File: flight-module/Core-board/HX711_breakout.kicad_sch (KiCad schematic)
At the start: 10 parts

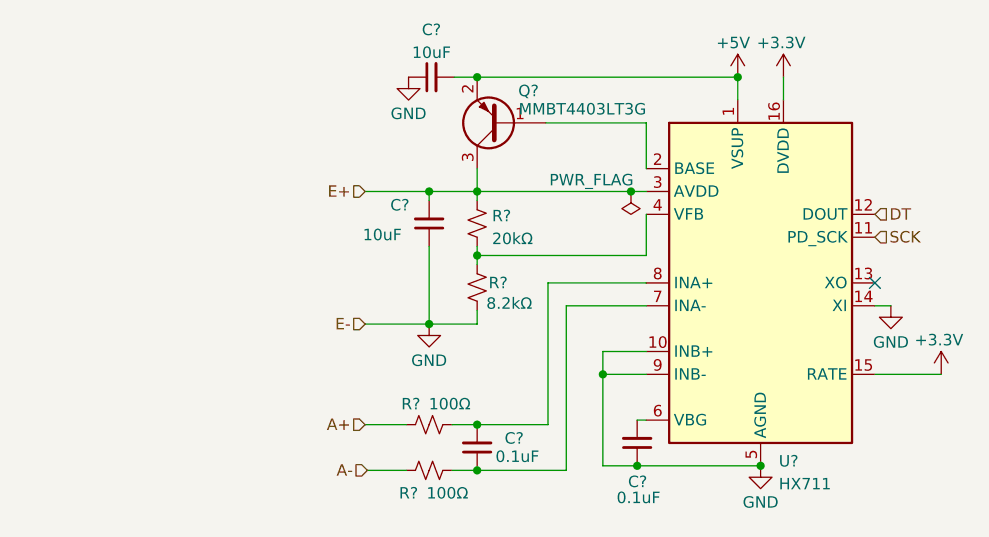
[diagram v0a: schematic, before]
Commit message: worked on core-board schematic. Not done.
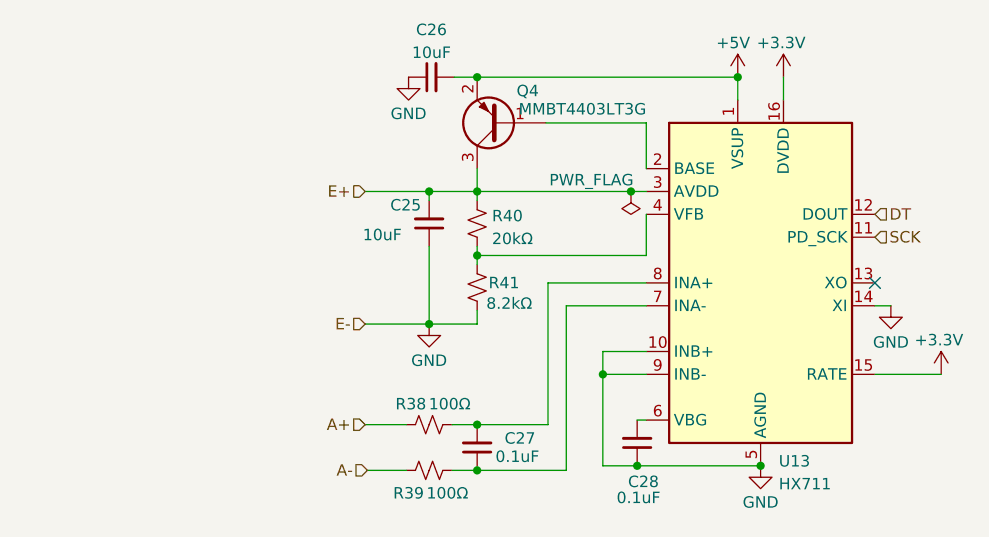
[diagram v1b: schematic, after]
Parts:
- gave numbers to parts that had none: 10

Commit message: Progress on core board.
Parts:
- added J5: Conn_01x03_Pin, Connector_PinHeader_2.54mm:PinHeader_1x03_P2.54mm_Vertical, symbol Connector:Conn_01x03_Pin
- renumbered C25 to C17, C26 to C18, C27 to C19, C28 to C20, R38 to R27, R39 to R28, R40 to R29, R41 to R30, U13 to U5
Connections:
- net A+: now also J5.3 (Pin_3)
- net E+: now also J5.1 (Pin_1)
- net GND: now also J5.2 (Pin_2)
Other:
- moved on the sheet: C17, C18, C20, Q4, R29, U5

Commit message: Finished flight-core.
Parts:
- added R1: 100kΩ, Resistor_SMD:R_0603_1608Metric, symbol Device:R_Small_US
- added R4: 2kΩ, Resistor_SMD:R_0603_1608Metric, symbol Device:R_Small_US
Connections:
- net A+: now also R1.1; no longer R27.2
- net GND: now also R4.1
- new net: R1.2, R27.2, R4.2
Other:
- moved on the sheet: J5
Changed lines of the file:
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@@
   (junction (at 116.84 40.64) (diameter 0) (color 0 0 0 0)
   )
+  (junction (at 76.2 68.58) (diameter 0) (color 0 0 0 0)
+  )
   (junction (at 86.36 60.96) (diameter 0) (color 0 0 0 0)
   )
@@
   )
   (junction (at 86.36 40.64) (diameter 0) (color 0 0 0 0)
+  )
+  (junction (at 76.2 78.74) (diameter 0) (color 0 0 0 0)
   )
   (junction (at 119.38 83.82) (diameter 0) (color 0 0 0 0)
@@
     (stroke (width 0) (type default))
   )
-  (wire (pts (xy 73.66 78.74) (xy 78.74 78.74))
-    (stroke (width 0) (type default))
-  )
   (wire (pts (xy 86.36 68.58) (xy 81.28 68.58))
     (stroke (width 0) (type default))
@@
     (stroke (width 0) (type default))
   )
-  (wire (pts (xy 73.66 68.58) (xy 81.28 68.58))
-    (stroke (width 0) (type default))
-  )
   (wire (pts (xy 86.36 60.96) (xy 106.68 60.96))
     (stroke (width 0) (type default))
@@
     (stroke (width 0) (type default))
   )
+  (wire (pts (xy 76.2 78.74) (xy 78.74 78.74))
+    (stroke (width 0) (type default))
+  )
   (wire (pts (xy 106.68 55.88) (xy 106.68 60.96))
     (stroke (width 0) (type default))
   )
+  (wire (pts (xy 76.2 68.58) (xy 76.2 71.12))
+    (stroke (width 0) (type default))
+  )
   (wire (pts (xy 86.36 40.64) (xy 116.84 40.64))
     (stroke (width 0) (type default))
@@
     (stroke (width 0) (type default))
   )
+  (wire (pts (xy 68.58 78.74) (xy 71.12 78.74))
+    (stroke (width 0) (type default))
+  )
   (wire (pts (xy 86.36 78.74) (xy 93.98 78.74))
     (stroke (width 0) (type default))
@@
     (stroke (width 0) (type default))
   )
+  (wire (pts (xy 76.2 76.2) (xy 76.2 78.74))
+    (stroke (width 0) (type default))
+  )
   (wire (pts (xy 86.36 53.34) (xy 104.14 53.34))
     (stroke (width 0) (type default))
@@
     (stroke (width 0) (type default))
   )
+  (wire (pts (xy 73.66 68.58) (xy 76.2 68.58))
+    (stroke (width 0) (type default))
+  )
   (wire (pts (xy 96.52 66.04) (xy 106.68 66.04))
     (stroke (width 0) (type default))
   )
+  (wire (pts (xy 76.2 68.58) (xy 81.28 68.58))
+    (stroke (width 0) (type default))
+  )
   (wire (pts (xy 104.14 83.82) (xy 119.38 83.82))
     (stroke (width 0) (type default))
@@
     (stroke (width 0) (type default))
   )
-  (hierarchical_label "E+" (shape input) (at 40.64 39.37 180) (fields_autoplaced)
+  (hierarchical_label "E+" (shape input) (at 40.64 40.64 180) (fields_autoplaced)
     (effects (font (size 1.27 1.27)) (justify right))
   )
-  (hierarchical_label "E-" (shape input) (at 40.64 41.91 180) (fields_autoplaced)
+  (hierarchical_label "E-" (shape input) (at 40.64 43.18 180) (fields_autoplaced)
     (effects (font (size 1.27 1.27)) (justify right))
   )
-  (hierarchical_label "A+" (shape input) (at 40.64 44.45 180) (fields_autoplaced)
-    (effects (font (size 1.27 1.27)) (justify right))
-  )
-  (hierarchical_label "A+" (shape input) (at 73.66 78.74 180) (fields_autoplaced)
+  (hierarchical_label "A+" (shape input) (at 40.64 45.72 180) (fields_autoplaced)
     (effects (font (size 1.27 1.27)) (justify right))
   )
@@
     (effects (font (size 1.27 1.27)) (justify right))
   )
+  (hierarchical_label "E+" (shape input) (at 73.66 53.34 180) (fields_autoplaced)
+    (effects (font (size 1.27 1.27)) (justify right))
+  )
+  (hierarchical_label "A+" (shape input) (at 68.58 78.74 180) (fields_autoplaced)
+    (effects (font (size 1.27 1.27)) (justify right))
+  )
+  (hierarchical_label "DT" (shape input) (at 132.08 55.88 0) (fields_autoplaced)
+    (effects (font (size 1.27 1.27)) (justify left))
+  )
   (hierarchical_label "E-" (shape input) (at 73.66 68.58 180) (fields_autoplaced)
     (effects (font (size 1.27 1.27)) (justify right))
   )
-  (hierarchical_label "E+" (shape input) (at 73.66 53.34 180) (fields_autoplaced)
-    (effects (font (size 1.27 1.27)) (justify right))
-  )
-  (hierarchical_label "DT" (shape input) (at 132.08 55.88 0) (fields_autoplaced)
-    (effects (font (size 1.27 1.27)) (justify left))
+  (symbol (lib_id "Device:R_Small_US") (at 73.66 78.74 90) (unit 1)
+    (in_bom yes) (on_board yes) (dnp no)
+    (property "Reference" "R1" (at 69.85 74.422 90)
+      (effects (font (size 1.27 1.27)))
+    )
+    (property "Value" "100kΩ" (at 70.358 76.454 90)
+      (effects (font (size 1.27 1.27)))
+    )
+    (property "Footprint" "Resistor_SMD:R_0603_1608Metric" (at 73.66 78.74 0)
+      (effects (font (size 1.27 1.27)) hide)
+    )
+    (property "Datasheet" "~" (at 73.66 78.74 0)
+      (effects (font (size 1.27 1.27)) hide)
+    )
+    (pin "1")
+    (pin "2")
+    (instances
+      (project "Core-board"
+        (path "/9e0a4b39-2b30-4bec-9684-92acf902e3a8"
+          (reference "R1") (unit 1)
+        )
+        (path "/9e0a4b39-2b30-4bec-9684-92acf902e3a8/b3294fa4-471e-45dc-a523-7ccd04494d78"
+          (reference "R39") (unit 1)
+        )
+        (path "/9e0a4b39-2b30-4bec-9684-92acf902e3a8/cd3938d8-ce4c-4959-93be-d4cb2465e0a1"
+          (reference "R1") (unit 1)
+        )
+        (path "/9e0a4b39-2b30-4bec-9684-92acf902e3a8/12b0e10d-9845-497e-abbc-bda1e9dd8c92"
+          (reference "R41") (unit 1)
+        )
+        (path "/9e0a4b39-2b30-4bec-9684-92acf902e3a8/cb63903c-f9f7-4011-8e67-b13383e994a7"
+          (reference "R43") (unit 1)
+        )
+        (path "/9e0a4b39-2b30-4bec-9684-92acf902e3a8/af93ca2d-dd0b-4d58-ab79-a2be12c29adf"
+          (reference "R45") (unit 1)
+        )
+        (path "/9e0a4b39-2b30-4bec-9684-92acf902e3a8/90940a16-eef6-4cc1-a4f4-72c883b01d02"
+          (reference "R47") (unit 1)
+        )
+      )
+    )
   )
   (symbol (lib_id "Device:C_Small") (at 81.28 40.64 90) (unit 1)
@@
     )
   )
-  (symbol (lib_id "Connector:Conn_01x03_Pin") (at 45.72 41.91 0) (mirror y) (unit 1)
-    (in_bom yes) (on_board yes) (dnp no)
-    (property "Reference" "J5" (at 45.085 35.1495 0)
-      (effects (font (size 1.27 1.27)))
-    )
-    (property "Value" "Conn_01x03_Pin" (at 45.085 37.5737 0)
-      (effects (font (size 1.27 1.27)))
-    )
-    (property "Footprint" "Connector_PinHeader_2.54mm:PinHeader_1x03_P2.54mm_Vertical" (at 45.72 41.91 0)
-      (effects (font (size 1.27 1.27)) hide)
-    )
-    (property "Datasheet" "~" (at 45.72 41.91 0)
+  (symbol (lib_id "Connector:Conn_01x03_Pin") (at 45.72 43.18 0) (mirror y) (unit 1)
+    (in_bom yes) (on_board yes) (dnp no)
+    (property "Reference" "J5" (at 45.085 36.4195 0)
+      (effects (font (size 1.27 1.27)))
+    )
+    (property "Value" "Conn_01x03_Pin" (at 45.085 38.8437 0)
+      (effects (font (size 1.27 1.27)))
+    )
+    (property "Footprint" "Connector_PinHeader_2.54mm:PinHeader_1x03_P2.54mm_Vertical" (at 45.72 43.18 0)
+      (effects (font (size 1.27 1.27)) hide)
+    )
+    (property "Datasheet" "~" (at 45.72 43.18 0)
       (effects (font (size 1.27 1.27)) hide)
     )
@@
         )
       )
+    )
+  )
+  (symbol (lib_id "Device:R_Small_US") (at 76.2 73.66 0) (unit 1)
+    (in_bom yes) (on_board yes) (dnp no)
+    (property "Reference" "R4" (at 72.136 70.866 0)
+      (effects (font (size 1.27 1.27)) (justify left))
+    )
+    (property "Value" "2kΩ" (at 71.374 72.644 0)
+      (effects (font (size 1.27 1.27)) (justify left))
+    )
+    (property "Footprint" "Resistor_SMD:R_0603_1608Metric" (at 76.2 73.66 0)
+      (effects (font (size 1.27 1.27)) hide)
+    )
+    (property "Datasheet" "~" (at 76.2 73.66 0)
+      (effects (font (size 1.27 1.27)) hide)
+    )
+    (pin "1")
+    (pin "2")
+    (instances
+      (project "Core-board"
+        (path "/9e0a4b39-2b30-4bec-9684-92acf902e3a8"
+          (reference "R4") (unit 1)
+        )
+        (path "/9e0a4b39-2b30-4bec-9684-92acf902e3a8/b3294fa4-471e-45dc-a523-7ccd04494d78"
+          (reference "R40") (unit 1)
+        )
+        (path "/9e0a4b39-2b30-4bec-9684-92acf902e3a8/cd3938d8-ce4c-4959-93be-d4cb2465e0a1"
+          (reference "R4") (unit 1)
+        )
+        (path "/9e0a4b39-2b30-4bec-9684-92acf902e3a8/12b0e10d-9845-497e-abbc-bda1e9dd8c92"
+          (reference "R42") (unit 1)
+        )
+        (path "/9e0a4b39-2b30-4bec-9684-92acf902e3a8/cb63903c-f9f7-4011-8e67-b13383e994a7"
+          (reference "R44") (unit 1)
+        )
+        (path "/9e0a4b39-2b30-4bec-9684-92acf902e3a8/af93ca2d-dd0b-4d58-ab79-a2be12c29adf"
+          (reference "R46") (unit 1)
+        )
+        (path "/9e0a4b39-2b30-4bec-9684-92acf902e3a8/90940a16-eef6-4cc1-a4f4-72c883b01d02"
+          (reference "R48") (unit 1)
+        )
+      )

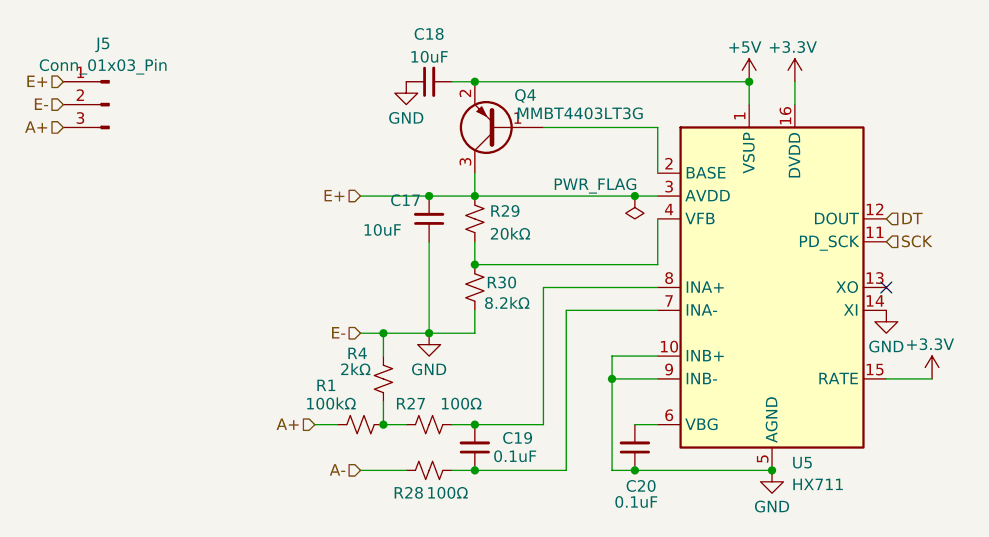
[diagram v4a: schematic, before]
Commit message: core board sd card and HX2 HX6 changes
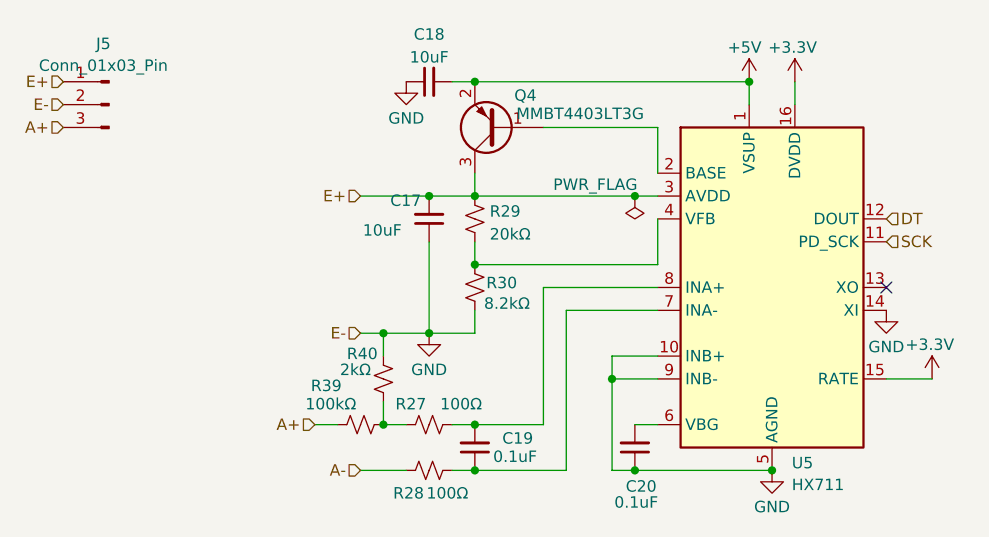
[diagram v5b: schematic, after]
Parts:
- renumbered R1 to R39, R4 to R40
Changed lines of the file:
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@@
   (symbol (lib_id "Device:R_Small_US") (at 73.66 78.74 90) (unit 1)
     (in_bom yes) (on_board yes) (dnp no)
-    (property "Reference" "R1" (at 69.85 74.422 90)
+    (property "Reference" "R39" (at 69.85 74.422 90)
       (effects (font (size 1.27 1.27)))
     )
@@
     (instances
       (project "Core-board"
-        (path "/9e0a4b39-2b30-4bec-9684-92acf902e3a8"
-          (reference "R1") (unit 1)
-        )
         (path "/9e0a4b39-2b30-4bec-9684-92acf902e3a8/b3294fa4-471e-45dc-a523-7ccd04494d78"
           (reference "R39") (unit 1)
@@
   (symbol (lib_id "Device:R_Small_US") (at 76.2 73.66 0) (unit 1)
     (in_bom yes) (on_board yes) (dnp no)
-    (property "Reference" "R4" (at 72.136 70.866 0)
+    (property "Reference" "R40" (at 72.136 70.866 0)
       (effects (font (size 1.27 1.27)) (justify left))
     )
@@
     (instances
       (project "Core-board"
-        (path "/9e0a4b39-2b30-4bec-9684-92acf902e3a8"
-          (reference "R4") (unit 1)
-        )
         (path "/9e0a4b39-2b30-4bec-9684-92acf902e3a8/b3294fa4-471e-45dc-a523-7ccd04494d78"
           (reference "R40") (unit 1)
